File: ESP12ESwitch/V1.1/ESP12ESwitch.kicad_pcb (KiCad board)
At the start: 2 copper layers, 16 parts, among them J1 Conn_01x06_Socket, J2 Conn_01x01_Pin, J3 B2+, J4 B1-, J5 B2-, J6 B1+, SW1 RST, SW2 BOOT, U1 ESP12E

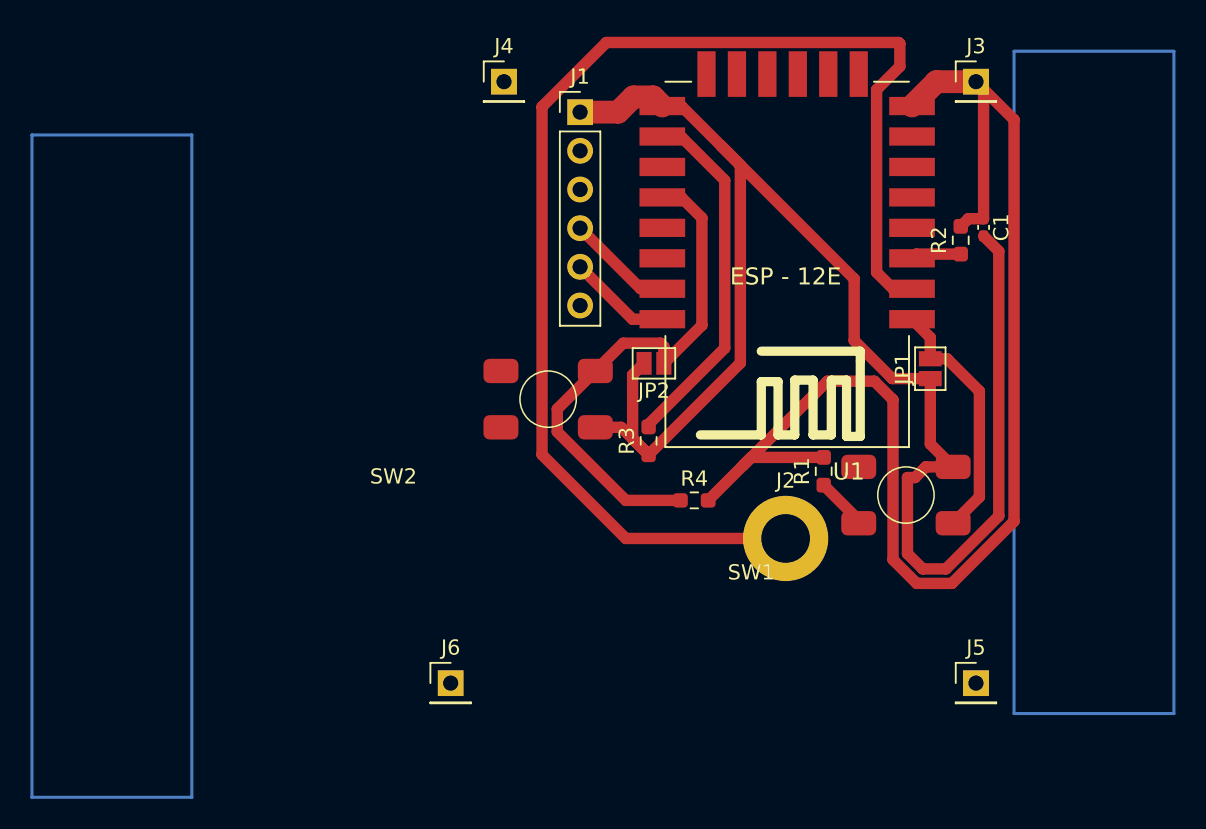
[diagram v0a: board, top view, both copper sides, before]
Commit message: began ESP32s2 based switch
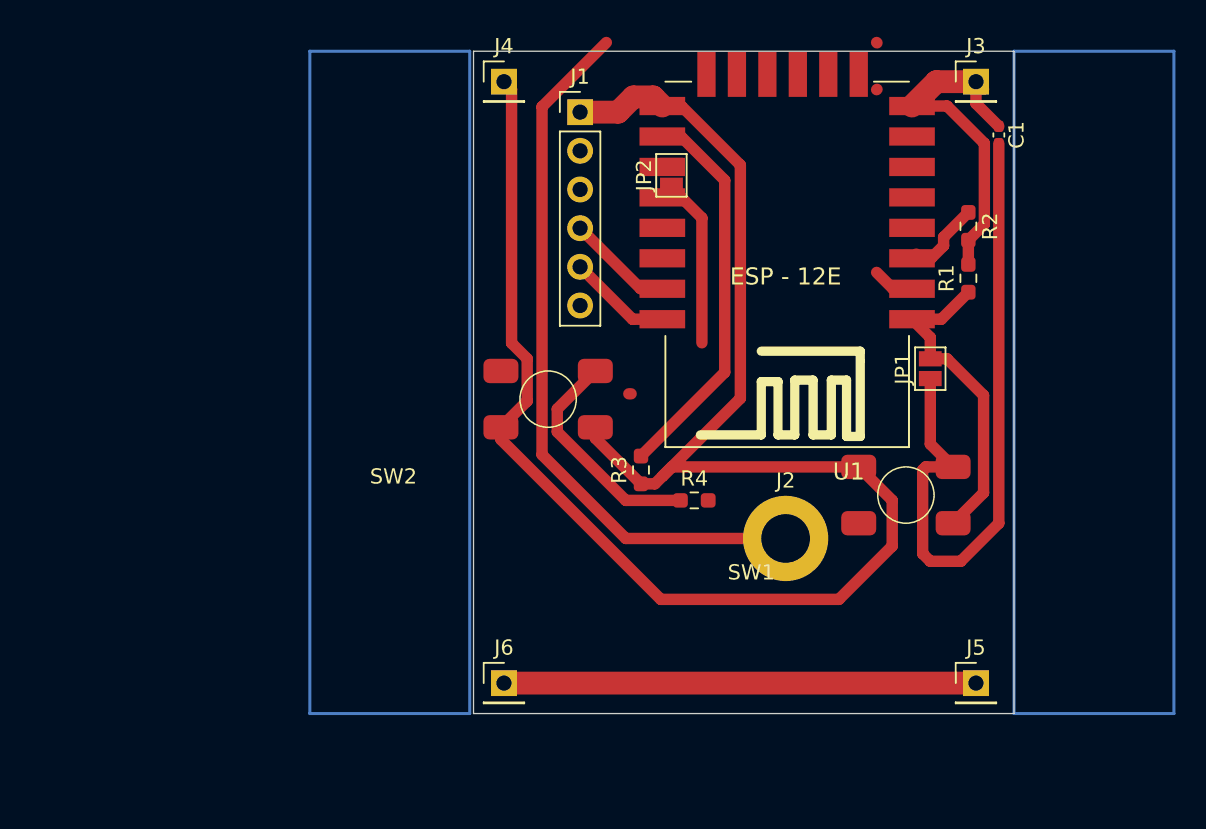
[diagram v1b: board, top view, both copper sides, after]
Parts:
- moved R1 15.8 mm to (112.0, 82.9)
- moved JP2 12.4 mm to (92.5, 76.2), turned to 90 degrees
- moved C1 6.15 mm to (114.0, 73.5)
- moved J6 3.50 mm to (81.5, 109.5)
- moved R3 1.98 mm to (90.5, 95.5)
- moved R2 1.04 mm to (112.0, 79.5), turned to -90 degrees
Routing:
- net /3V: track 87.9 -> 23.3 mm
- net /GND: track 109.1 -> 162.8 mm
- net Net-(J2-Pin_1): track 84.8 -> 49.9 mm
- net Net-(J5-Pin_1): track 0.00 -> 31.0 mm
- net Net-(JP2-A): track 35.2 -> 26.3 mm
- net Net-(R2-Pad1): track 3.31 -> 5.67 mm
- net Net-(R3-Pad2): track 23.6 -> 25.7 mm
- net Net-(JP1-B): track 20.0 -> 21.5 mm
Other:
- board outline added: 35.5 x 43.5 mm
